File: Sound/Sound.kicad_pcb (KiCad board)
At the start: 2 copper layers, 133.6 x 74.7 mm, 7 parts, among them J1 Expansion_Connector, U1 74HCT74, U2 74HCT08, U3 74HCT21, U4 74HCT04

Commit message: Bug fixes...
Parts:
- added J2: AudioJack3_Ground, Connector_Audio:Jack_3.5mm_CUI_SJ1-3533NG_Horizontal, F.Cu at (158.5, 58.9)
- added J3: AudioJack2_Ground, Connector_Audio:Jack_3.5mm_CUI_SJ1-3533NG_Horizontal, F.Cu at (168.7, 58.9)
- added RV1: R_POT_Dual_Separate, Potentiometer_THT:Potentiometer_Piher_T-16H_Double_Horizontal, F.Cu at (136.2, 66.5)
- added RV3: R_POT, Potentiometer_THT:Potentiometer_Piher_T-16H_Single_Horizontal, F.Cu at (128.7, 84.0)
- added U5: LM386, Package_DIP:DIP-8_W7.62mm_Socket_LongPads, F.Cu at (148.0, 74.9)
- added U6: LM386, Package_DIP:DIP-8_W7.62mm_Socket_LongPads, F.Cu at (159.8, 74.9)
- added U7: LM386, Package_DIP:DIP-8_W7.62mm_Socket_LongPads, F.Cu at (176.0, 54.8)
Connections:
- SOUND_GEN1 pad 15: (no net) -> Net-(RV1-Pad4)
- SOUND_GEN1 pad 17: (no net) -> Net-(RV1-Pad1)
- SOUND_GEN1 pad 18: (no net) -> Net-(RV3-Pad1)

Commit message: Updated documentation location...
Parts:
- added C1: CP, Capacitor_THT:CP_Radial_D5.0mm_P2.50mm, F.Cu at (141.6, 64.6)
- added C2: C, Capacitor_THT:C_Disc_D3.0mm_W2.0mm_P2.50mm, F.Cu at (138.4, 63.1)
- added C3: CP, Capacitor_THT:CP_Radial_D5.0mm_P2.50mm, F.Cu at (142.5, 59.1)
- added C4: C, Capacitor_THT:C_Disc_D3.0mm_W2.0mm_P2.50mm, F.Cu at (143.9, 53.6)
- added C5: CP, Capacitor_THT:CP_Radial_D5.0mm_P2.50mm, F.Cu at (172.7, 66.9)
- added C6: C, Capacitor_THT:C_Disc_D3.0mm_W2.0mm_P2.50mm, F.Cu at (175.9, 59.2)
- J2: value AudioJack3_Ground -> LINE OUT
- J3: value AudioJack2_Ground -> SUB OUT
- moved RV1 84.8 mm to (53.7, 86.1), turned to 180 degrees
- moved U7 74.9 mm to (129.0, 113.2)
- moved U5 51.9 mm to (113.0, 113.2)
- moved U6 41.0 mm to (144.9, 113.0)
- moved RV3 31.6 mm to (137.7, 53.7), turned to 90 degrees
- moved U4 29.8 mm to (142.7, 84.5), turned to 180 degrees
- moved U1 16.1 mm to (167.0, 120.9)
- moved J2 7.83 mm to (151.0, 56.6)
- moved U3 6.44 mm to (135.3, 88.8)
- moved J3 5.48 mm to (163.8, 56.5)
- renumbered YamahaSound1 to SOUND_CTRL1
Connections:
- J1 pad 30: ~IRQ3 -> (no net)
- J2 pad R: (no net) -> SND_R
- J2 pad T: (no net) -> SND_L
- J3 pad T: (no net) -> SND_SUB
- SOUND_CTRL1 pad 21: ~IRQ3 -> (no net)
- U5 pad 5: (no net) -> Net-(C1-Pad1)
- U6 pad 5: (no net) -> Net-(C3-Pad1)
- U7 pad 5: (no net) -> Net-(C5-Pad1)
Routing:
- net GND: track 0.00 -> 453.7 mm
- net VCC: track 0.00 -> 250.5 mm
- net ~RESET: track 0.00 -> 184.5 mm, vias 0 -> 4
- net Net-(RV3-Pad1): track 0.00 -> 168.3 mm, vias 0 -> 3
- net A0: track 0.00 -> 130.8 mm, vias 0 -> 5
- net A1: track 0.00 -> 129.9 mm, vias 0 -> 1
- net R\~W: track 0.00 -> 128.9 mm, vias 0 -> 3
- net Net-(RV1-Pad5): track 0.00 -> 115.1 mm, vias 0 -> 4
- net Net-(C5-Pad1): track 0.00 -> 113.4 mm, vias 0 -> 5
- net 2MHz: track 0.00 -> 90.3 mm, vias 0 -> 1
- net Net-(RV1-Pad2): track 0.00 -> 85.5 mm, vias 0 -> 1
- net Net-(C3-Pad1): track 0.00 -> 83.0 mm, vias 0 -> 3
- net Net-(C1-Pad1): track 0.00 -> 80.6 mm, vias 0 -> 3
- net Net-(RV3-Pad2): track 0.00 -> 69.1 mm, vias 0 -> 1
- net A7: track 0.00 -> 59.8 mm, vias 0 -> 2
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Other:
- copper layers 2 -> 4
- board text added: "WN-6502-WBC Sound Card"

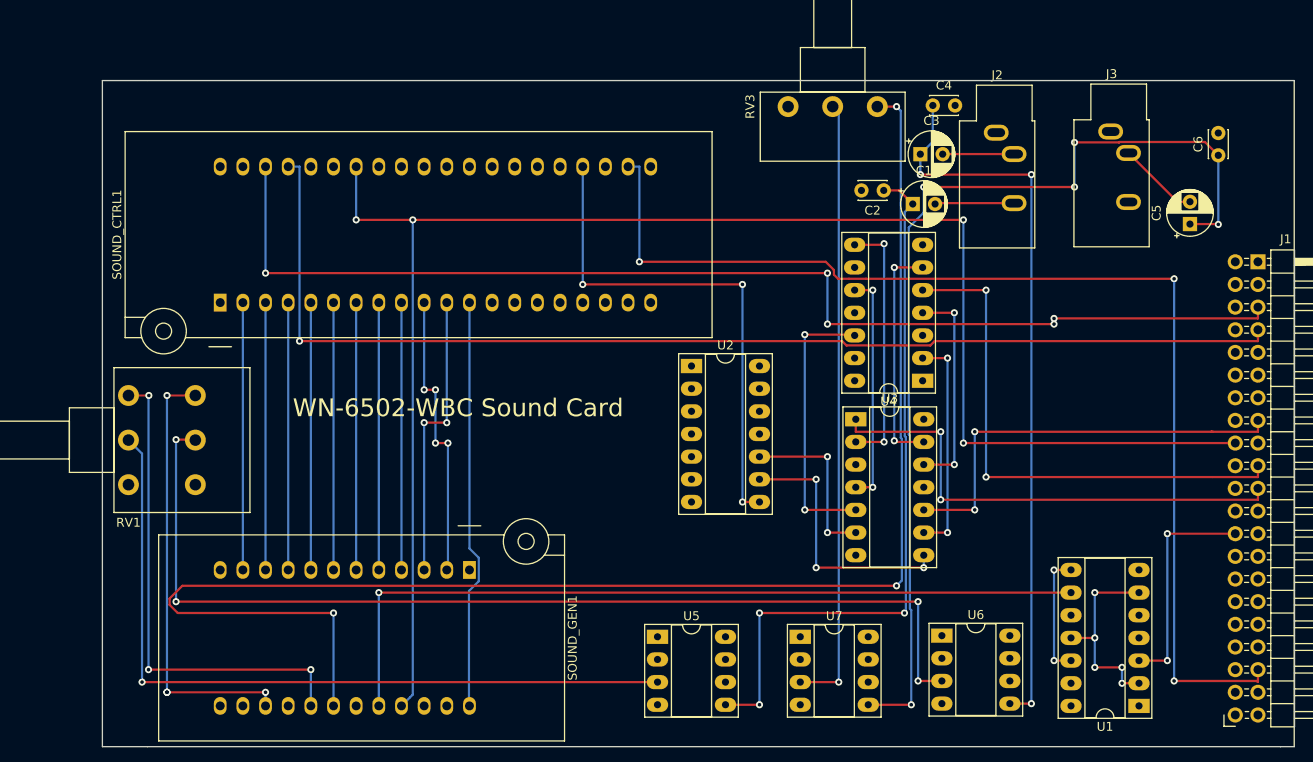
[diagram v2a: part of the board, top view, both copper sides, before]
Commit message: Renamed some components...
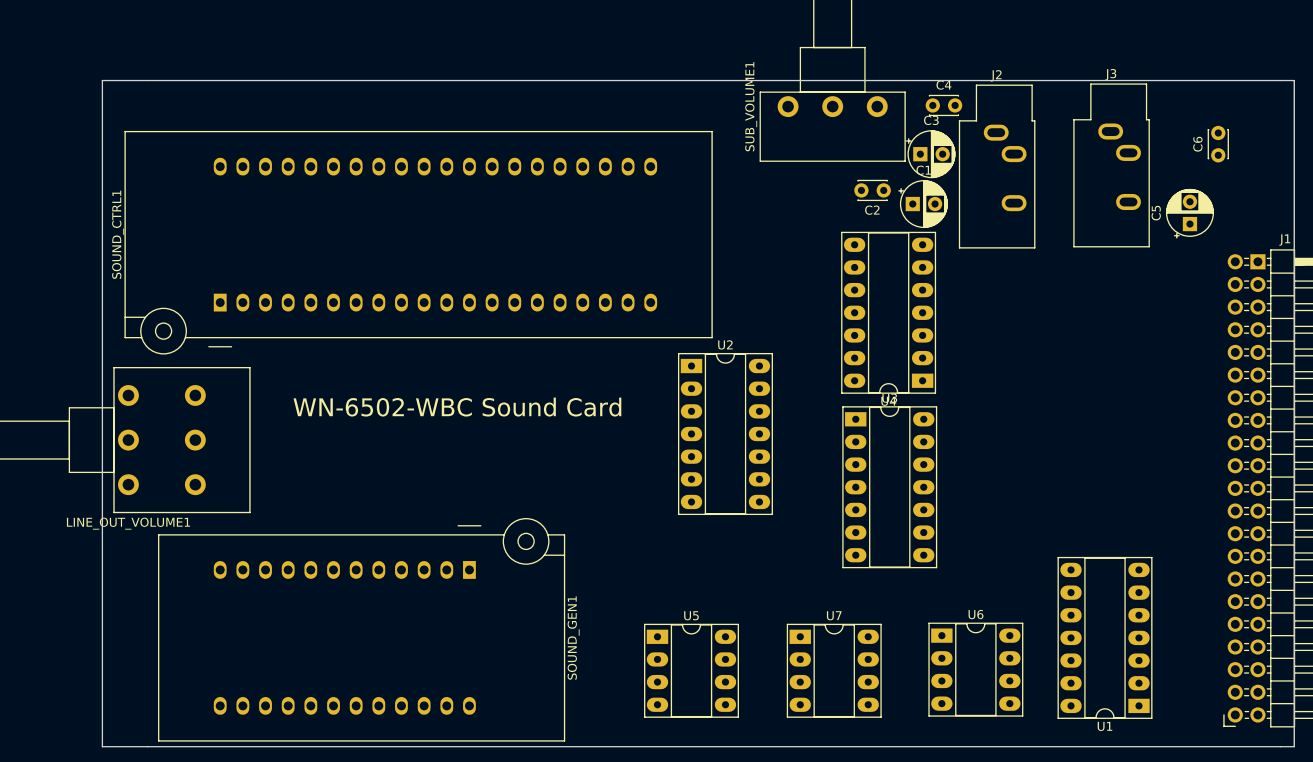
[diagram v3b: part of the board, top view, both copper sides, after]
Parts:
- LINE_OUT_VOLUME1: renamed from RV1; value R_POT_Dual_Separate -> LINE OUT VOLUME
- renumbered RV3 to SUB_VOLUME1
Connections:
- U1 pad 14: (no net) -> VCC
- U1 pad 7: (no net) -> GND
- U2 pad 14: (no net) -> VCC
- U2 pad 7: (no net) -> GND
- U3 pad 14: (no net) -> VCC
- U3 pad 7: (no net) -> GND
- U4 pad 14: (no net) -> VCC
- U4 pad 7: (no net) -> GND
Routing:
- net GND: track 453.7 -> 0.00 mm
- net VCC: track 250.5 -> 0.00 mm
- net ~RESET: track 184.5 -> 0.00 mm, vias 4 -> 0
- net Net-(SOUND_GEN1-Pad18): track 168.3 -> 0.00 mm, vias 3 -> 0
- net A0: track 130.8 -> 0.00 mm, vias 5 -> 0
- net A1: track 129.9 -> 0.00 mm, vias 1 -> 0
- net R\~W: track 128.9 -> 0.00 mm, vias 3 -> 0
- net Net-(LINE_OUT_VOLUME1-Pad5): track 115.1 -> 0.00 mm, vias 4 -> 0
- net Net-(C5-Pad1): track 113.4 -> 0.00 mm, vias 5 -> 0
- net 2MHz: track 90.3 -> 0.00 mm, vias 1 -> 0
- net Net-(LINE_OUT_VOLUME1-Pad2): track 85.5 -> 0.00 mm, vias 1 -> 0
- net Net-(C3-Pad1): track 83.0 -> 0.00 mm, vias 3 -> 0
- net Net-(C1-Pad1): track 80.6 -> 0.00 mm, vias 3 -> 0
- net Net-(SUB_VOLUME1-Pad2): track 69.1 -> 0.00 mm, vias 1 -> 0
- net A7: track 59.8 -> 0.00 mm, vias 2 -> 0
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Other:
- copper layers 4 -> 6

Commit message: Sound card schematic completed...
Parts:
- added C10: 10 µF, Capacitor_THT:CP_Radial_D5.0mm_P2.50mm, F.Cu at (205.2, 86.7)
- added C11: 0.1 µF, Capacitor_THT:C_Disc_D3.0mm_W2.0mm_P2.50mm, F.Cu at (222.2, 117.2)
- added C12: 0.033 µF, Capacitor_THT:C_Disc_D3.0mm_W2.0mm_P2.50mm, F.Cu at (222.6, 82.5)
- added C7: 0.1 µF, Capacitor_THT:C_Disc_D3.0mm_W2.0mm_P2.50mm, F.Cu at (211.3, 85.5)
- added C8: 10 µF, Capacitor_THT:CP_Radial_D5.0mm_P2.50mm, F.Cu at (213.3, 80.4)
- added C9: 0.1 µF, Capacitor_THT:C_Disc_D3.0mm_W2.0mm_P2.50mm, F.Cu at (219.4, 78.9)
- added R1: 10 Ω, Resistor_THT:R_Axial_DIN0204_L3.6mm_D1.6mm_P5.08mm_Horizontal, F.Cu at (231.1, 74.5)
- added R2: 10 Ω, Resistor_THT:R_Axial_DIN0204_L3.6mm_D1.6mm_P5.08mm_Horizontal, F.Cu at (199.3, 58.8)
- added R3: 10 Ω, Resistor_THT:R_Axial_DIN0204_L3.6mm_D1.6mm_P5.08mm_Horizontal, F.Cu at (208.9, 53.2)
- added R4: ? Ω, Resistor_THT:R_Axial_DIN0204_L3.6mm_D1.6mm_P5.08mm_Horizontal, F.Cu at (204.6, 78.7)
- added R5: 10 Ω, Resistor_THT:R_Axial_DIN0204_L3.6mm_D1.6mm_P5.08mm_Horizontal, F.Cu at (231.0, 131.1)
- C1, C3, C5: value CP -> 250 µF
- C2, C4, C6: value C -> 0.05 µF
- LINE_OUT_VOLUME1: value LINE OUT VOLUME -> 10k Ω
- SUB_VOLUME1: value R_POT -> 10k Ω
- moved C2 98.7 mm to (236.4, 74.5)
- moved C3 98.7 mm to (240.5, 70.4)
- moved U3 98.7 mm to (233.3, 100.1)
- moved U4 98.7 mm to (240.8, 95.8)
- moved U5 98.7 mm to (211.1, 124.5)
- moved C1 98.7 mm to (239.7, 75.9)
- moved U1 98.7 mm to (265.0, 132.2)
- moved U2 98.7 mm to (214.9, 94.1)
- moved U6 98.7 mm to (243.0, 124.3)
- moved U7 98.7 mm to (227.1, 124.5)
- moved C4 97.3 mm to (240.5, 64.9)
- moved J3 86.0 mm to (77.9, 56.0)
- moved J2 86.0 mm to (65.0, 56.1)
- moved SUB_VOLUME1 85.1 mm to (53.7, 67.9), turned to 180 degrees
- moved SOUND_CTRL1 83.6 mm to (147.4, 70.5), turned to 0 degrees
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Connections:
- C2 pad 2: GND -> Net-(C2-Pad2)
- C4 pad 2: GND -> Net-(C4-Pad2)
- C6 pad 2: GND -> Net-(C6-Pad2)
- U5 pad 1: (no net) -> Net-(C8-Pad1)
- U5 pad 7: (no net) -> Net-(C7-Pad2)
- U5 pad 8: (no net) -> Net-(C8-Pad2)
- U6 pad 1: (no net) -> Net-(C10-Pad1)
- U6 pad 7: (no net) -> Net-(C9-Pad2)
- U6 pad 8: (no net) -> Net-(C10-Pad2)
- U7 pad 1: (no net) -> Net-(R5-Pad2)
- U7 pad 7: (no net) -> Net-(C11-Pad2)
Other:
- copper layers 6 -> 4

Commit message: Completed Sound Card...
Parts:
- added REF**: OSHW-Logo_11.4x12mm_SilkScreen, Symbol:OSHW-Logo_11.4x12mm_SilkScreen, F.Cu at (174.4, 60.4)
- added REF**: WEEE-Logo_4.2x6mm_SilkScreen, Symbol:WEEE-Logo_4.2x6mm_SilkScreen, F.Cu at (104.1, 116.5)
- added REF**: CE-Logo_8.5x6mm_SilkScreen, Symbol:CE-Logo_8.5x6mm_SilkScreen, F.Cu at (112.7, 116.4)
- added REF**: KiCad-Logo2_6mm_SilkScreen, Symbol:KiCad-Logo2_6mm_SilkScreen, F.Cu at (128.2, 116.3)
- moved C4 188.4 mm to (56.0, 103.0)
- moved C3 180.9 mm to (63.0, 105.0)
- moved U6 174.4 mm to (70.0, 102.0)
- moved U7 164.7 mm to (70.0, 75.0)
- moved U1 160.1 mm to (114.0, 79.0)
- moved C1 152.1 mm to (87.8, 68.5), turned to 180 degrees
- moved R5 151.8 mm to (92.0, 70.0)
- moved C9 151.7 mm to (72.0, 115.0)
- moved C11 149.9 mm to (85.0, 57.0)
- moved U5 145.7 mm to (70.0, 88.0)
- moved U3 139.2 mm to (95.0, 84.0)
- moved C2 138.4 mm to (98.4, 64.3), turned to 0 degrees
- moved C7 136.6 mm to (78.0, 115.0)
- moved R2 134.0 mm to (66.0, 73.0)
- moved U2 132.1 mm to (83.0, 86.0)
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- renumbered J2 to LINE_OUT1, J3 to SUB_OUT1
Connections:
- R4 pad 1: (no net) -> SND_SUB
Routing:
- net GND: track 0.00 -> 350.9 mm
- net VCC: track 0.00 -> 238.5 mm
- net A7: track 0.00 -> 165.8 mm
- net A10: track 0.00 -> 129.0 mm
- net A6: track 0.00 -> 126.0 mm, vias 0 -> 1
- net A9: track 0.00 -> 117.8 mm
- net A8: track 0.00 -> 116.8 mm
- net 8MHz: track 0.00 -> 91.3 mm, vias 0 -> 2
- net Net-(LINE_OUT_VOLUME1-Pad4): track 0.00 -> 90.3 mm, vias 0 -> 4
- net A5: track 0.00 -> 90.2 mm, vias 0 -> 2
- net A11: track 0.00 -> 88.8 mm
- net Net-(SOUND_GEN1-Pad18): track 0.00 -> 85.0 mm
- net Net-(SOUND_CTRL1-Pad24): track 0.00 -> 83.8 mm, vias 0 -> 2
- net A4: track 0.00 -> 72.9 mm
- net Net-(LINE_OUT_VOLUME1-Pad1): track 0.00 -> 71.7 mm, vias 0 -> 2
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- added copper zone on GND.Cu, net GND
- added copper zone on VCC.Cu, net VCC

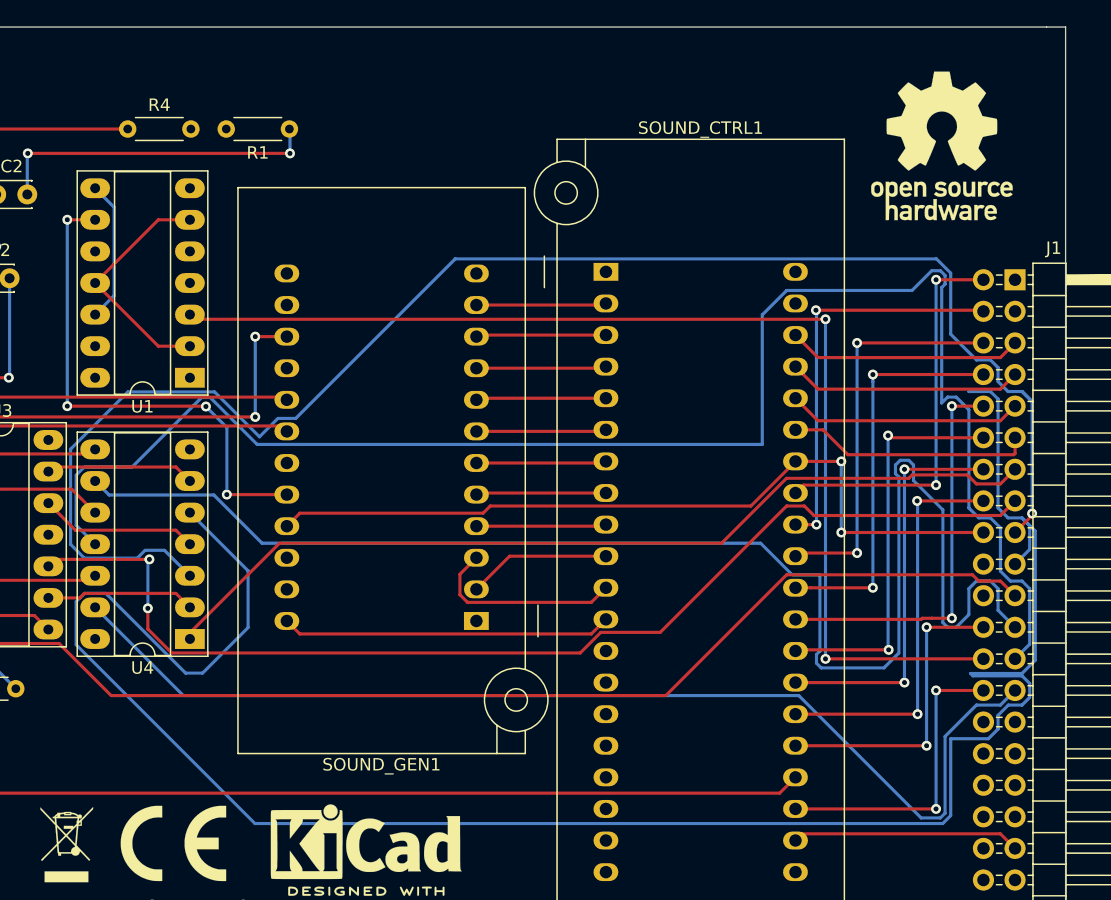
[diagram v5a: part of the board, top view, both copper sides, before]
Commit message: Updated motherboard PCB and finished sound card PCB...
Website added to PCB design and completed sound card schematic, PCB and SVG files.
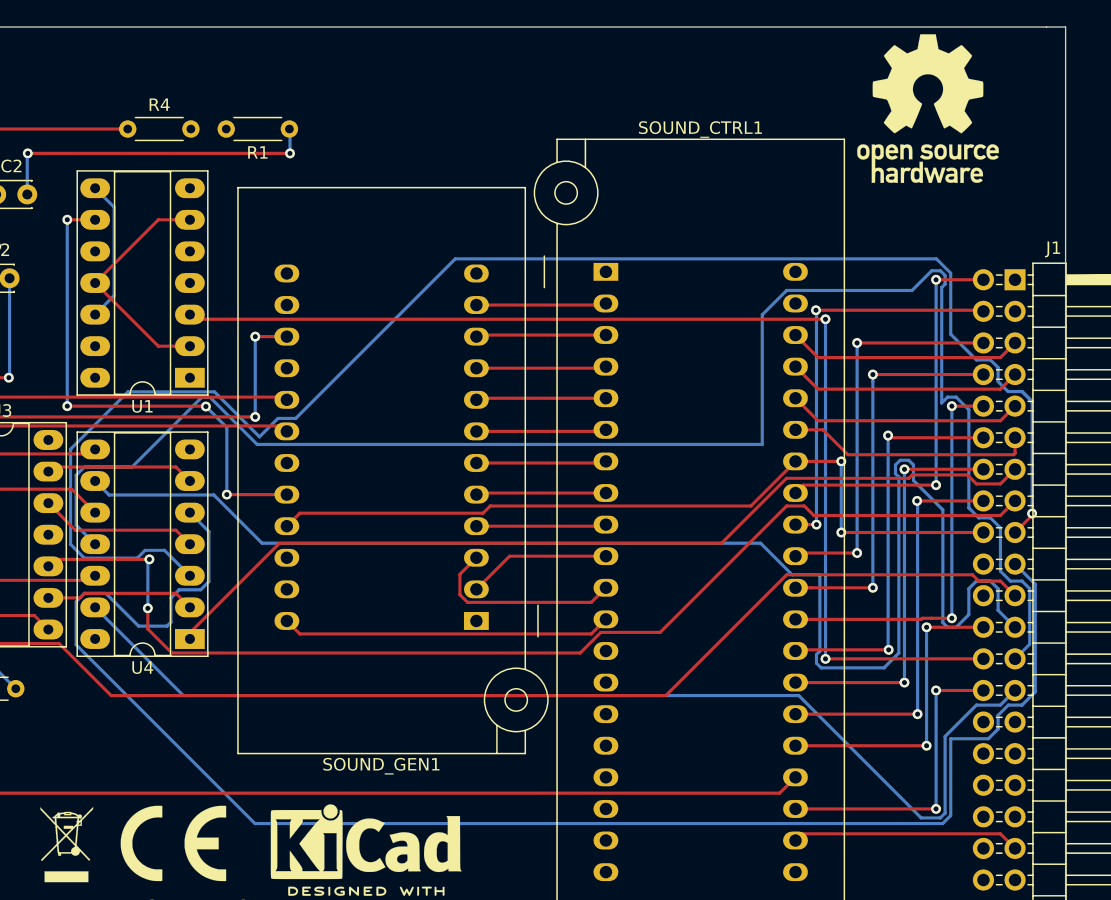
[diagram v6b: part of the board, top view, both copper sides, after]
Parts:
- moved REF** 3.20 mm to (173.3, 57.4)
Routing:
- net A7: track 165.8 -> 127.0 mm
- removed copper zone on GND.Cu, net GND
- removed copper zone on VCC.Cu, net VCC
